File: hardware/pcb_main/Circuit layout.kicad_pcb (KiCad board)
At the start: 4 copper layers, 93 x 45 mm, 72 parts, among them J1 687108149022, J2 PH1-06-UA, J3 FTSH-105-01-L-DV-K, J4 PH1-12-UA, U1 1016TR, U2 DQN0004A-MFG, U3 LM27761, U4 ADS1299IPAGR, U5 nRF52832-QFxx, Y1 32MHz

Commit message: All done, main and bridge 4 done
final push for a while
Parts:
- removed C6, C7: 1uF, Capacitor_SMD:C_0402_1005Metric_Pad0.74x0.62mm_HandSolder
- removed D1: BAT30F4, foots:BAT30F4
- removed R1: 6.34K, Resistor_SMD:R_0402_1005Metric_Pad0.72x0.64mm_HandSolder
- removed R2: 10K, Resistor_SMD:R_0402_1005Metric_Pad0.72x0.64mm_HandSolder
- removed the TP2 at (86.2, 123.6)
- added L5: 2.2uH, foots:DFE252012F-2R2M=P2, F.Cu at (101.3, 99.5)
- added PS1: TPS613222ADBVT, foots:TPS613222ADBVT, F.Cu at (97.1, 102.0)
- added TP1: GND, TestPoint:TestPoint_Pad_D2.0mm, B.Cu at (124.5, 113.5)
- added TP3: 5V, TestPoint:TestPoint_Pad_D2.0mm, B.Cu at (94.7, 108.5)
- C4: value 1uF -> 33uF; footprint Capacitor_SMD:C_0402_1005Metric_Pad0.74x0.62mm_HandSolder -> Capacitor_SMD:C_0805_2012Metric
- C5: value 4.7uF -> 33uF; footprint Capacitor_SMD:C_0402_1005Metric_Pad0.74x0.62mm_HandSolder -> Capacitor_SMD:C_0805_2012Metric
- TP2: renamed from TP1; moved to B.Cu
- U2: value DQN0004A-MFG -> TPS7A2030PDQNR
- U3: value LM27761 -> CDBU0130L; footprint foots:LM27761DSGT -> foots:CDBU0130L
- moved TP2 14.7 mm to (103.6, 116.2)
- moved U3 10.8 mm to (108.8, 106.0), turned to -90 degrees
- moved C3 6.39 mm to (98.4, 98.4), turned to -135 degrees
- moved C4 6.02 mm to (101.6, 105.2), turned to 45 degrees
- moved FM2 2.50 mm to (107.5, 95.0)
- moved C5 2.19 mm to (99.5, 103.9), turned to 45 degrees
- moved FM1 1.52 mm to (136.6, 102.9)
- moved L3 1.25 mm to (118.5, 91.5), turned to 90 degrees
- moved C21 1.06 mm to (116.3, 102.2), turned to -45 degrees
- moved C1 0.20 mm to (107.2, 106.0)
- moved C19 0.20 mm to (96.5, 105.6)
- moved C32 0.20 mm to (96.5, 106.8)
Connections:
- C12 pad 2: -2V -> GND
- C13 pad 1: -2V -> GND
- C14 pad 2: -2V -> GND
- C15 pad 2: -2V -> GND
- C16 pad 2: -2V -> GND
- C18 pad 1: -2V -> GND
- C19 pad 2: -2V -> GND
- C29 pad 1: +3V -> +5V
- C29 pad 2: -2V -> GND
- C30 pad 1: +3V -> +5V
- C30 pad 2: -2V -> GND
- C31 pad 1: +3V -> +5V
- C31 pad 2: -2V -> GND
- C32 pad 1: +3V -> +5V
- C32 pad 2: -2V -> GND
- C33 pad 1: +3V -> +5V
- C33 pad 2: -2V -> GND
- C4 pad 1: /C+ -> +5V
- C4 pad 2: /C- -> GND
- C5 pad 1: /CPOUT -> +5V
- J1 pad 3: -2V -> GND
- J1 pad 6: -2V -> GND
- J1 pad MP1: -2V -> GND
- J1 pad MP2: -2V -> GND
- L3 pad 1: GND -> /RF_ANT
- L3 pad 2: /RF_ANT -> unconnected-(L3-NC-Pad2)
- U3 pad 2: GND -> /PWR_D
- U4 pad 1: +3V -> +5V
- U4 pad 10: +3V -> +5V
- U4 pad 12: +3V -> +5V
- U4 pad 14: +3V -> +5V
- U4 pad 16: +3V -> +5V
- U4 pad 17: -2V -> GND
- U4 pad 19: +3V -> +5V
- U4 pad 2: +3V -> +5V
- U4 pad 20: -2V -> GND
- U4 pad 21: +3V -> +5V
- U4 pad 22: +3V -> +5V
- U4 pad 23: -2V -> GND
- U4 pad 25: -2V -> GND
- U4 pad 3: +3V -> +5V
- U4 pad 32: -2V -> GND
- U4 pad 4: +3V -> +5V
- U4 pad 5: +3V -> +5V
- U4 pad 53: -2V -> GND
- U4 pad 54: +3V -> +5V
- U4 pad 56: +3V -> +5V
- U4 pad 57: -2V -> GND
- U4 pad 58: -2V -> GND
- U4 pad 59: +3V -> +5V
- U4 pad 6: +3V -> +5V
- U4 pad 7: +3V -> +5V
- U4 pad 8: +3V -> +5V
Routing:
- net GND: track 1.50 -> 63.8 mm, vias 22 -> 348
- net +5V: track 0.00 -> 38.3 mm, vias 0 -> 4
- net +3V: track 10.9 -> 49.2 mm, vias 12 -> 9
- net +PWR: track 41.9 -> 22.2 mm, vias 4 -> 2
- net -2V: track 9.12 -> 0.00 mm, vias 48 -> 0
- net /RF_ANT: track 0.00 -> 2.55 mm
- net /PWR_D: track 16.5 -> 15.4 mm
- net /GPIO13: track 3.35 -> 4.06 mm
- net /GPIO20: track 22.5 -> 23.1 mm
- net /GPIO24: track 35.8 -> 35.3 mm
- net /GPIO14: track 6.65 -> 6.89 mm, vias 0 -> 1
- added copper zone on F.Cu, net +5V
- added copper zone on F.Cu, net /SW
- added copper zone on B.Cu, net GND
- added copper zone on F.Cu, net GND
- added copper zone on In1.Cu, net GND
- removed copper zone on B.Cu, net -2V
- removed copper zone on F.Cu, net -2V
- removed copper zone on In1.Cu, net -2V
- removed copper zone on F.Cu, net /C+
- removed copper zone on F.Cu, net /C-
- removed copper zone on F.Cu, net /CPOUT
- removed copper zone on F.Cu, net /RF_ANT
- removed copper zone on F.Cu, net /VFB
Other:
- board size 93 x 45 mm -> 91 x 43 mm
- board text added: "+3V"
- board text added: "+5V"
- board text added: "A"
- board text added: "GND"
- board text added: "N"

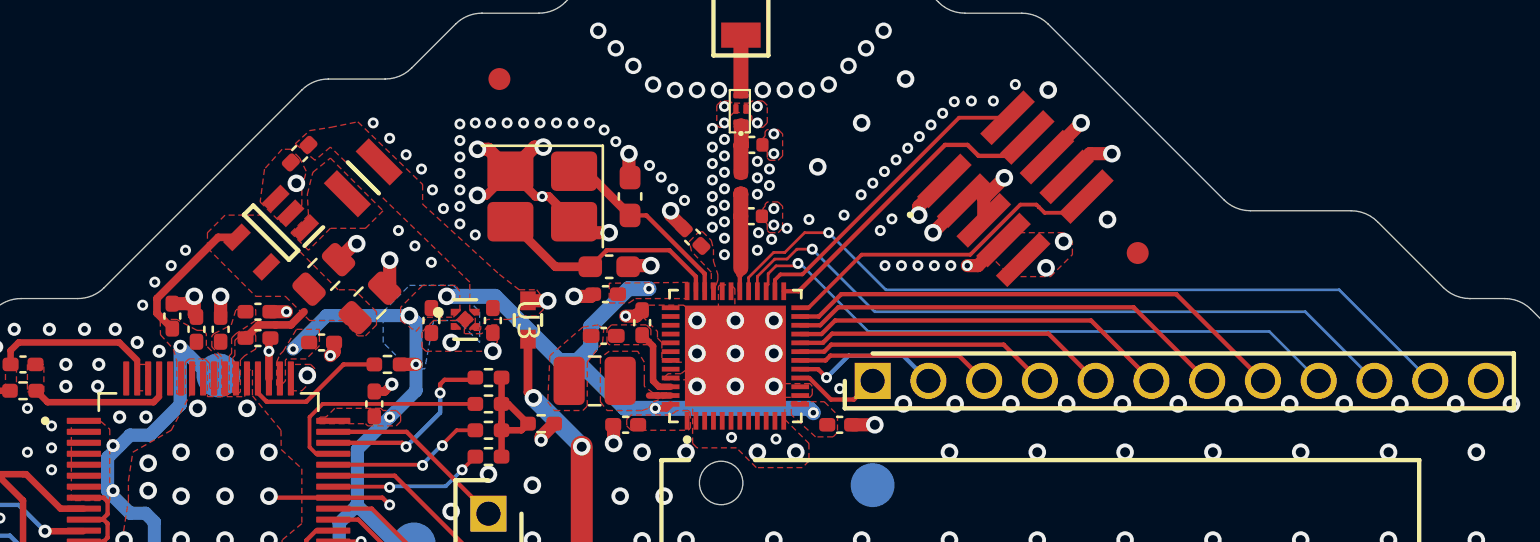
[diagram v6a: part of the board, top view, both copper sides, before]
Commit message: Final push for now
All bridges ordered, main DAQ ordered,
Main DAQ needed 1 tweak to prevent short circuit due to close by traces
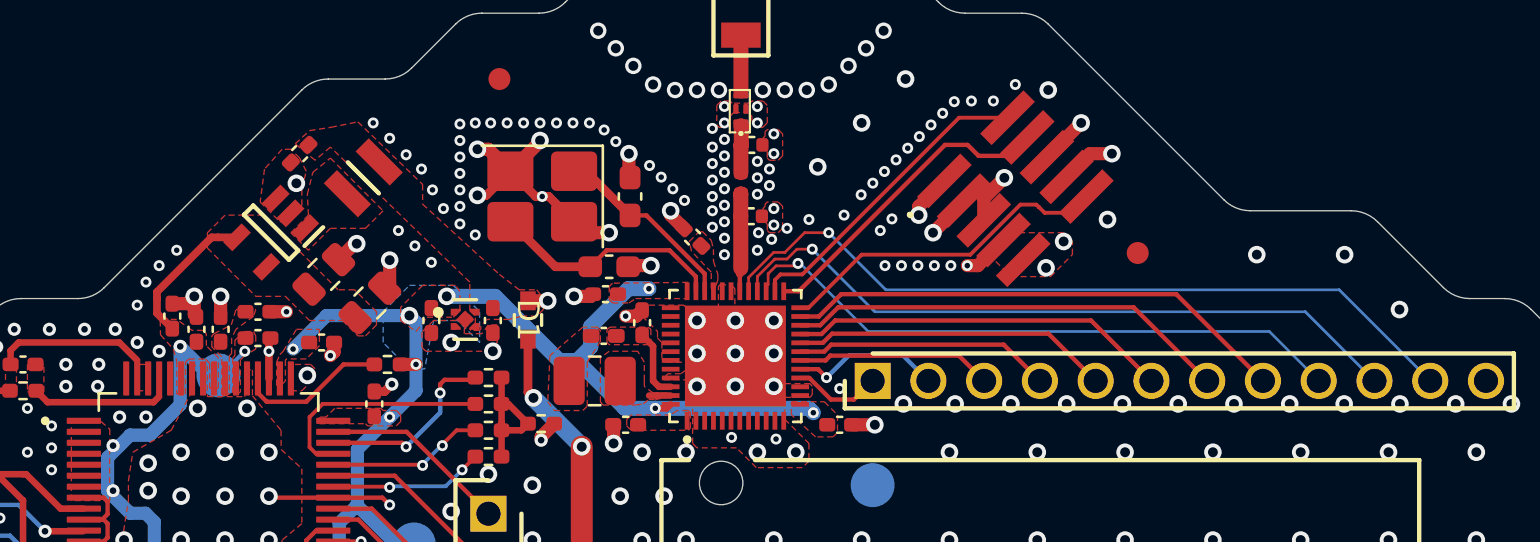
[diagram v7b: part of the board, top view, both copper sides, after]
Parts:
- renumbered C12 to C10, C13 to C11, C14 to C12, C15 to C13, C16 to C14, C17 to C15, C18 to C16, C19 to C17, C20 to C18, C21 to C19, C22 to C20, C23 to C21, C24 to C22, C25 to C23, C26 to C24, C27 to C25, C28 to C26, C29 to C27, C30 to C28, C31 to C29, C32 to C30, C33 to C31, C34 to C32, C35 to C33, C8 to C6, C9 to C7, C10 to C8, C11 to C9, U3 to D1, L5 to L1, L1 to L2, L2 to L3, L3 to L4, L4 to L5, PS1 to U3
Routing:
- net +5V: track 38.3 -> 37.0 mm, vias 4 -> 5
- net GND: vias 348 -> 351
